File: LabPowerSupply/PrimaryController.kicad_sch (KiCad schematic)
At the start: 16 parts

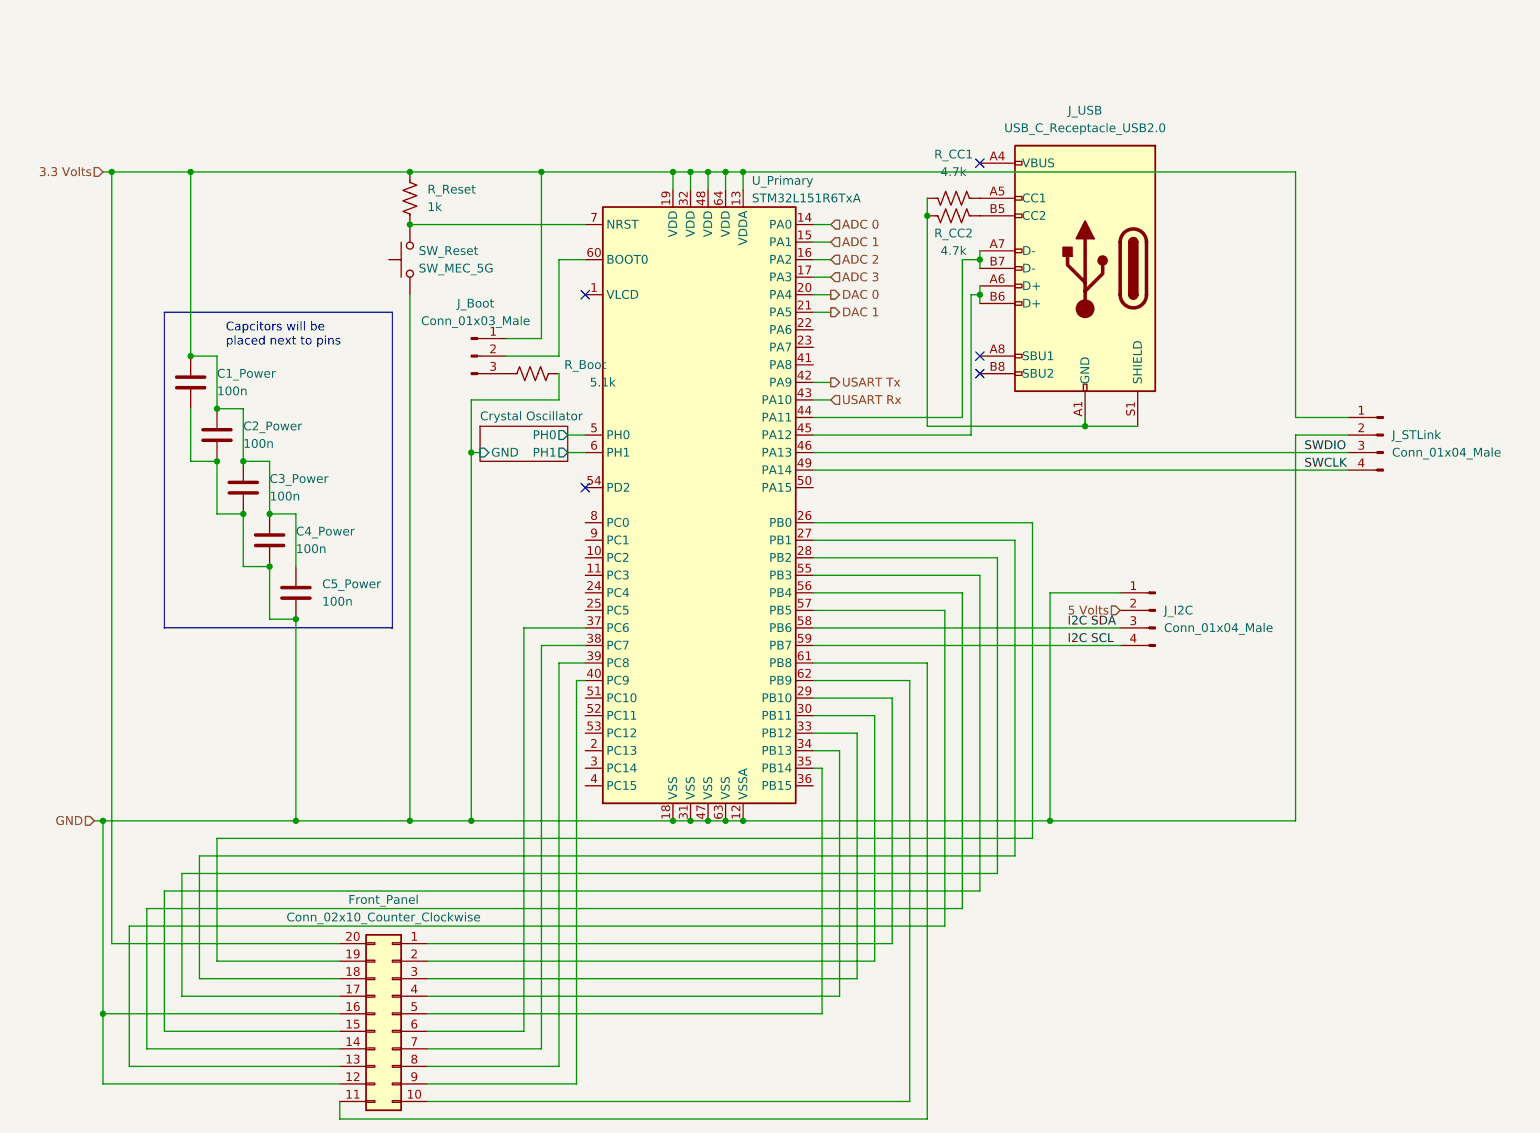
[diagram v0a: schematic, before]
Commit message: Finished first pass on the schematic
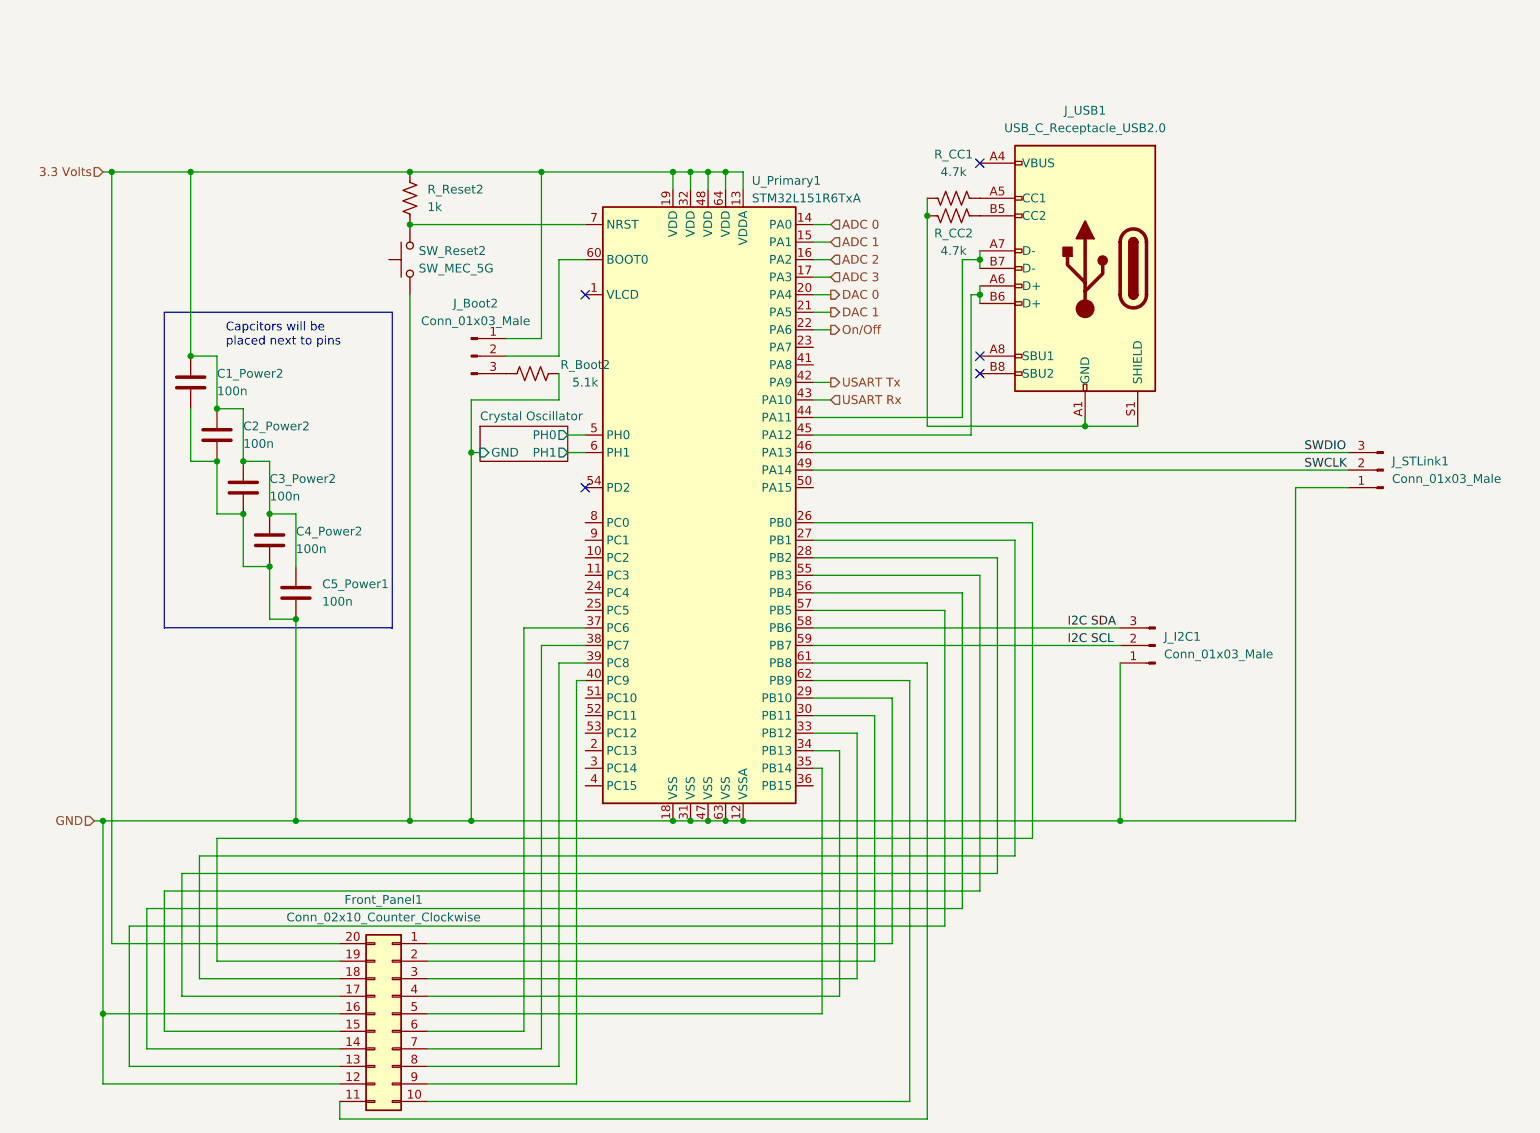
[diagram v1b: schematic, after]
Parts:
- removed J_I2C, J_STLink: Conn_01x04_Male, Connector_JST:JST_EH_B4B-EH-A_1x04_P2.50mm_Vertical, symbol Connector:Conn_01x04_Male
- added J_I2C1, J_STLink1: Conn_01x03_Male, Connector_PinHeader_2.54mm:PinHeader_1x03_P2.54mm_Vertical, symbol Connector:Conn_01x03_Male
- renumbered C1_Power to C1_Power2, C2_Power to C2_Power2, C3_Power to C3_Power2, C4_Power to C4_Power2, C5_Power to C5_Power1, Front_Panel to Front_Panel1, J_Boot to J_Boot2, J_USB to J_USB1, R_Boot to R_Boot2, R_Reset to R_Reset2, SW_Reset to SW_Reset2, U_Primary to U_Primary1
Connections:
- net GND: now also J_I2C1.1 (Pin_1), J_STLink1.1 (Pin_1)
- net I2C SCL: now also J_I2C1.2 (Pin_2)
- net I2C SDA: now also J_I2C1.3 (Pin_3)
- net SWCLK: now also J_STLink1.2 (Pin_2)
- net SWDIO: now also J_STLink1.3 (Pin_3)
- net On/Off: now reaches U_Primary1.22 (PA6)

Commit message: started PCB
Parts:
- J_Boot2: footprint (none) -> Connector_PinHeader_2.54mm:PinHeader_1x03_P2.54mm_Vertical
- R_Reset2: footprint (none) -> Resistor_SMD:R_1210_3225Metric
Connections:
- net GND: now also J_I2C1.3 (Pin_3), J_STLink1.3 (Pin_3); no longer J_I2C1.1 (Pin_1), J_STLink1.1 (Pin_1)
- net I2C SDA: now also J_I2C1.1 (Pin_1); no longer J_I2C1.3 (Pin_3)
- net SWDIO: now also J_STLink1.1 (Pin_1); no longer J_STLink1.3 (Pin_3)
- no-connect marks 5 -> 21
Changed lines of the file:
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@@
   (no_connect (at 160.02 35.56))
   (no_connect (at 102.87 82.55))
+  (no_connect (at 102.87 113.03))
+  (no_connect (at 102.87 125.73))
+  (no_connect (at 102.87 123.19))
+  (no_connect (at 102.87 120.65))
+  (no_connect (at 102.87 118.11))
+  (no_connect (at 102.87 115.57))
+  (no_connect (at 102.87 100.33))
+  (no_connect (at 102.87 97.79))
+  (no_connect (at 102.87 95.25))
+  (no_connect (at 102.87 92.71))
+  (no_connect (at 102.87 90.17))
+  (no_connect (at 102.87 87.63))
+  (no_connect (at 135.89 62.23))
+  (no_connect (at 135.89 64.77))
+  (no_connect (at 135.89 125.73))
+  (no_connect (at 135.89 82.55))
   (no_connect (at 102.87 54.61))
   (wire (pts (xy 67.31 148.59) (xy 34.29 148.59))
@@
     (stroke (width 0) (type default) (color 0 0 0 0))
   )
-  (wire (pts (xy 175.26 73.66) (xy 175.26 72.39))
-    (stroke (width 0) (type default) (color 0 0 0 0))
-  )
   (wire (pts (xy 158.75 54.61) (xy 160.02 54.61))
     (stroke (width 0) (type default) (color 0 0 0 0))
@@
     (effects (font (size 1.27 1.27)) (justify left))
   )
-  (symbol (lib_id "Connector:Conn_01x03_Male") (at 218.44 80.01 180) (unit 1)
+  (symbol (lib_id "Connector:Conn_01x03_Male") (at 218.44 80.01 0) (mirror y) (unit 1)
     (in_bom yes) (on_board yes) (fields_autoplaced)
     (property "Reference" "J_STLink1" (id 0) (at 219.71 78.7399 0)
@@
     )
     (property "Datasheet" "~" (id 3) (at 218.44 80.01 0)
+      (effects (font (size 1.27 1.27)) hide)
+    )
+    (pin "1")
+    (pin "2")
+    (pin "3")
+  )
+  (symbol (lib_id "Connector:Conn_01x03_Male") (at 185.42 105.41 0) (mirror y) (unit 1)
+    (in_bom yes) (on_board yes) (fields_autoplaced)
+    (property "Reference" "J_I2C1" (id 0) (at 186.69 104.1399 0)
+      (effects (font (size 1.27 1.27)) (justify right))
+    )
+    (property "Value" "Conn_01x03_Male" (id 1) (at 186.69 106.6799 0)
+      (effects (font (size 1.27 1.27)) (justify right))
+    )
+    (property "Footprint" "Connector_PinHeader_2.54mm:PinHeader_1x03_P2.54mm_Vertical" (id 2) (at 185.42 105.41 0)
+      (effects (font (size 1.27 1.27)) hide)
+    )
+    (property "Datasheet" "~" (id 3) (at 185.42 105.41 0)
       (effects (font (size 1.27 1.27)) hide)
     )
@@
       (effects (font (size 1.27 1.27)) (justify left))
     )
-    (property "Footprint" "" (id 2) (at 78.486 40.894 90)
+    (property "Footprint" "Resistor_SMD:R_1210_3225Metric" (id 2) (at 78.486 40.894 90)
       (effects (font (size 1.27 1.27)) hide)
     )
@@
     (pin "1")
     (pin "2")
-  )
-  (symbol (lib_id "Connector:Conn_01x03_Male") (at 185.42 105.41 180) (unit 1)
-    (in_bom yes) (on_board yes) (fields_autoplaced)
-    (property "Reference" "J_I2C1" (id 0) (at 186.69 104.1399 0)
-      (effects (font (size 1.27 1.27)) (justify right))
-    )
-    (property "Value" "Conn_01x03_Male" (id 1) (at 186.69 106.6799 0)
-      (effects (font (size 1.27 1.27)) (justify right))
-    )
-    (property "Footprint" "Connector_PinHeader_2.54mm:PinHeader_1x03_P2.54mm_Vertical" (id 2) (at 185.42 105.41 0)
-      (effects (font (size 1.27 1.27)) hide)
-    )
-    (property "Datasheet" "~" (id 3) (at 185.42 105.41 0)
-      (effects (font (size 1.27 1.27)) hide)
-    )
-    (pin "1")
-    (pin "2")
-    (pin "3")
   )
   (symbol (lib_id "Device:R_US") (at 156.21 40.64 270) (mirror x) (unit 1)
@@
     (property "Reference" "J_Boot2" (id 0) (at 86.995 55.88 0))
     (property "Value" "Conn_01x03_Male" (id 1) (at 86.995 58.42 0))
-    (property "Footprint" "" (id 2) (at 86.36 63.5 0)
-      (effects (font (size 1.27 1.27)) hide)
-    )
+    (property "Footprint" "Connector_PinHeader_2.54mm:PinHeader_1x03_P2.54mm_Vertical" (id 2) (at 86.36 63.5 0)
+      (effects (font (size 1.27 1.27)) hide)
+    )

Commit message: more work
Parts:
- added C1_Y1, C2_Y1: 100n, Capacitor_SMD:C_1210_3225Metric, symbol Device:C
- added Y1: 8M, Crystal:Crystal_HC18-U_Vertical, symbol Device:Crystal
- Front_Panel1: footprint Connector_JST:JST_PHD_B20B-PHDSS_2x10_P2.00mm_Vertical -> Connector_IDC:IDC-Header_2x10_P2.54mm_Vertical
- renumbered C1_Power2 to C1_Power1, C2_Power2 to C2_Power1, C3_Power2 to C3_Power1, C4_Power2 to C4_Power1, J_Boot2 to J_Boot1, U_Primary1 to MCU_1, R_Boot2 to R_Boot1, R_Reset2 to R_Reset1, SW_Reset2 to SW_Reset1
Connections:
- net GND: now also C1_Y1.1, C2_Y1.1
- net Crystal Oscillator/PH0: no longer names the net of MCU_1.5 (PH0)
- net Crystal Oscillator/PH0: now also C1_Y1.2, Y1.2
- net Crystal Oscillator/PH1: no longer names the net of MCU_1.6 (PH1)
- net Crystal Oscillator/PH1: now also C2_Y1.2, Y1.1
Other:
- removed sheet Crystal Oscillator
- moved on the sheet: C5_Power1
